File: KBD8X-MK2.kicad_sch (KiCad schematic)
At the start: 26 parts, among them J1 AVR-ISP-6, Q1 DSS60601MZ4-13, SW1 SW_Push, U1 ATmega32U4-MU, U2 PRTR5V0U2X, Y1 16MHz

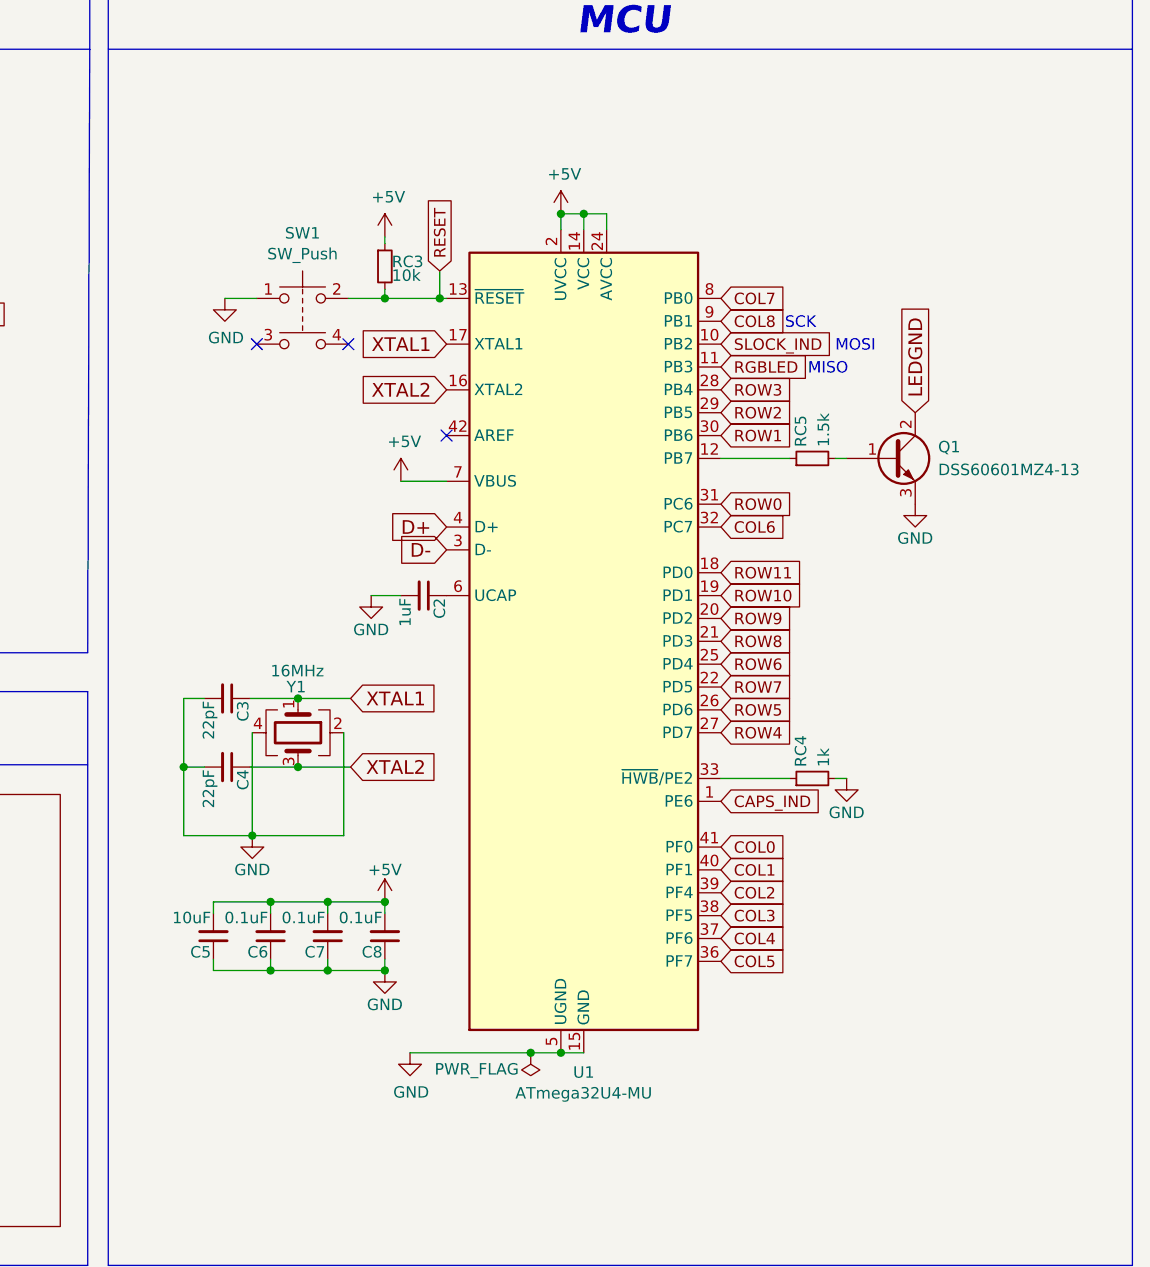
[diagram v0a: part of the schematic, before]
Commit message: Removed leds and unnecessary resistors
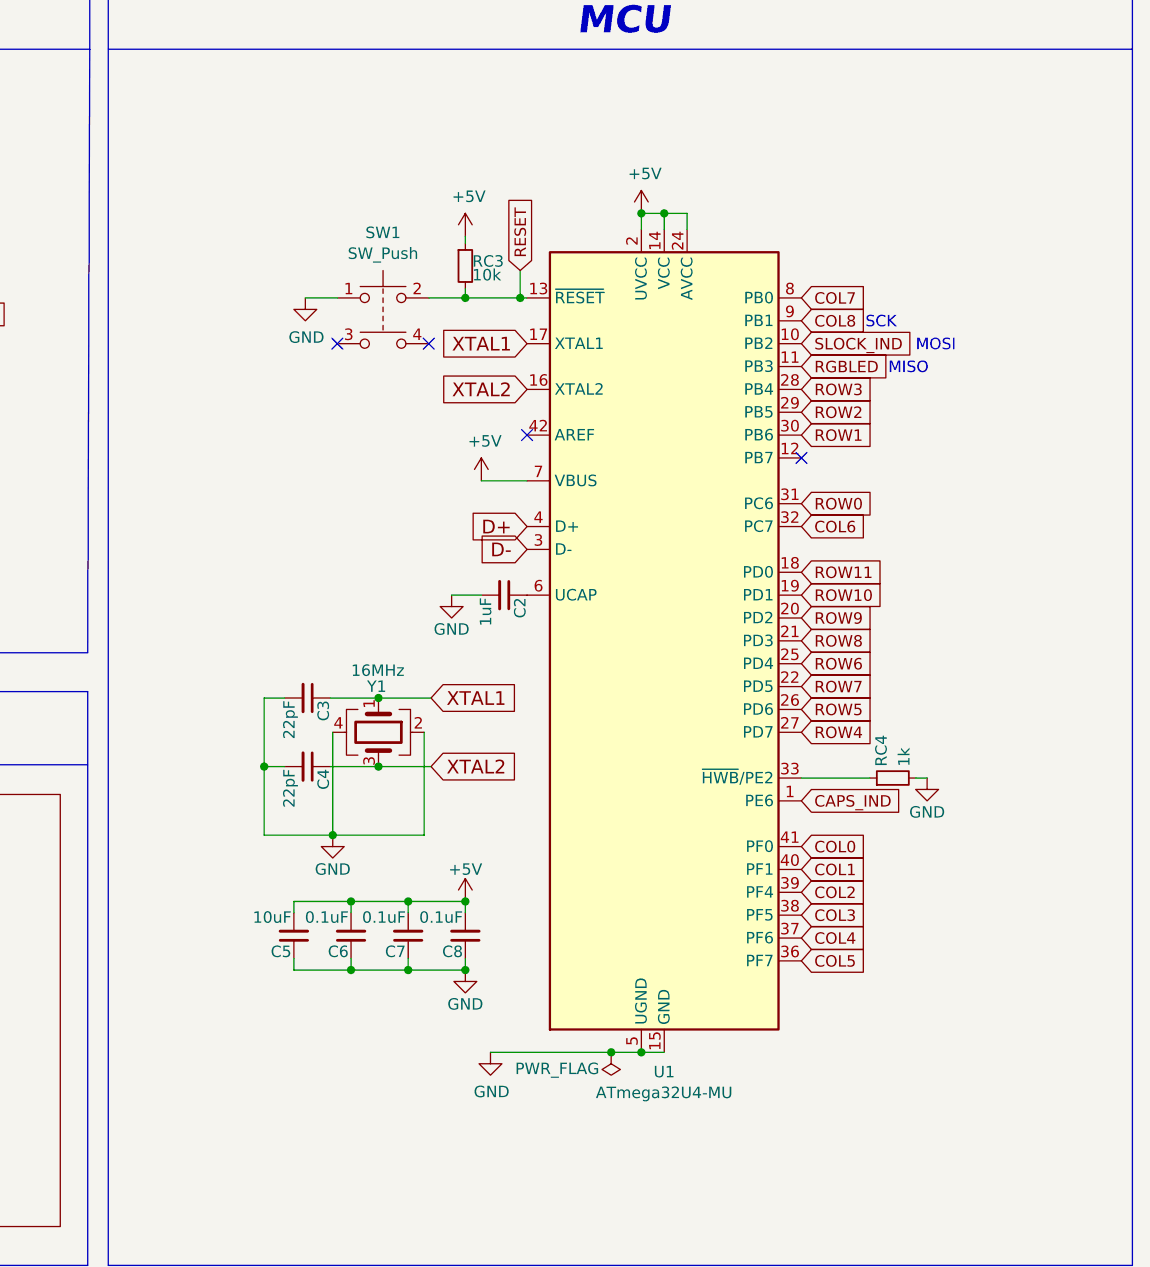
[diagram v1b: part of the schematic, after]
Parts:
- removed Q1: DSS60601MZ4-13, KBD8X_MK2_Components:SOT-223-3_TabPin2, symbol KBD8X_MK2_Components:Q_NPN_BCE
- removed RC5: 1.5k, KBD8X_MK2_Components:R_0603, symbol KBD8X_MK2_Components:R_Small
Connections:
- no-connect marks 5 -> 6
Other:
- moved on the sheet: C2, C3, C4, C5, C6, C7, C8, RC3, RC4, SW1, U1, Y1

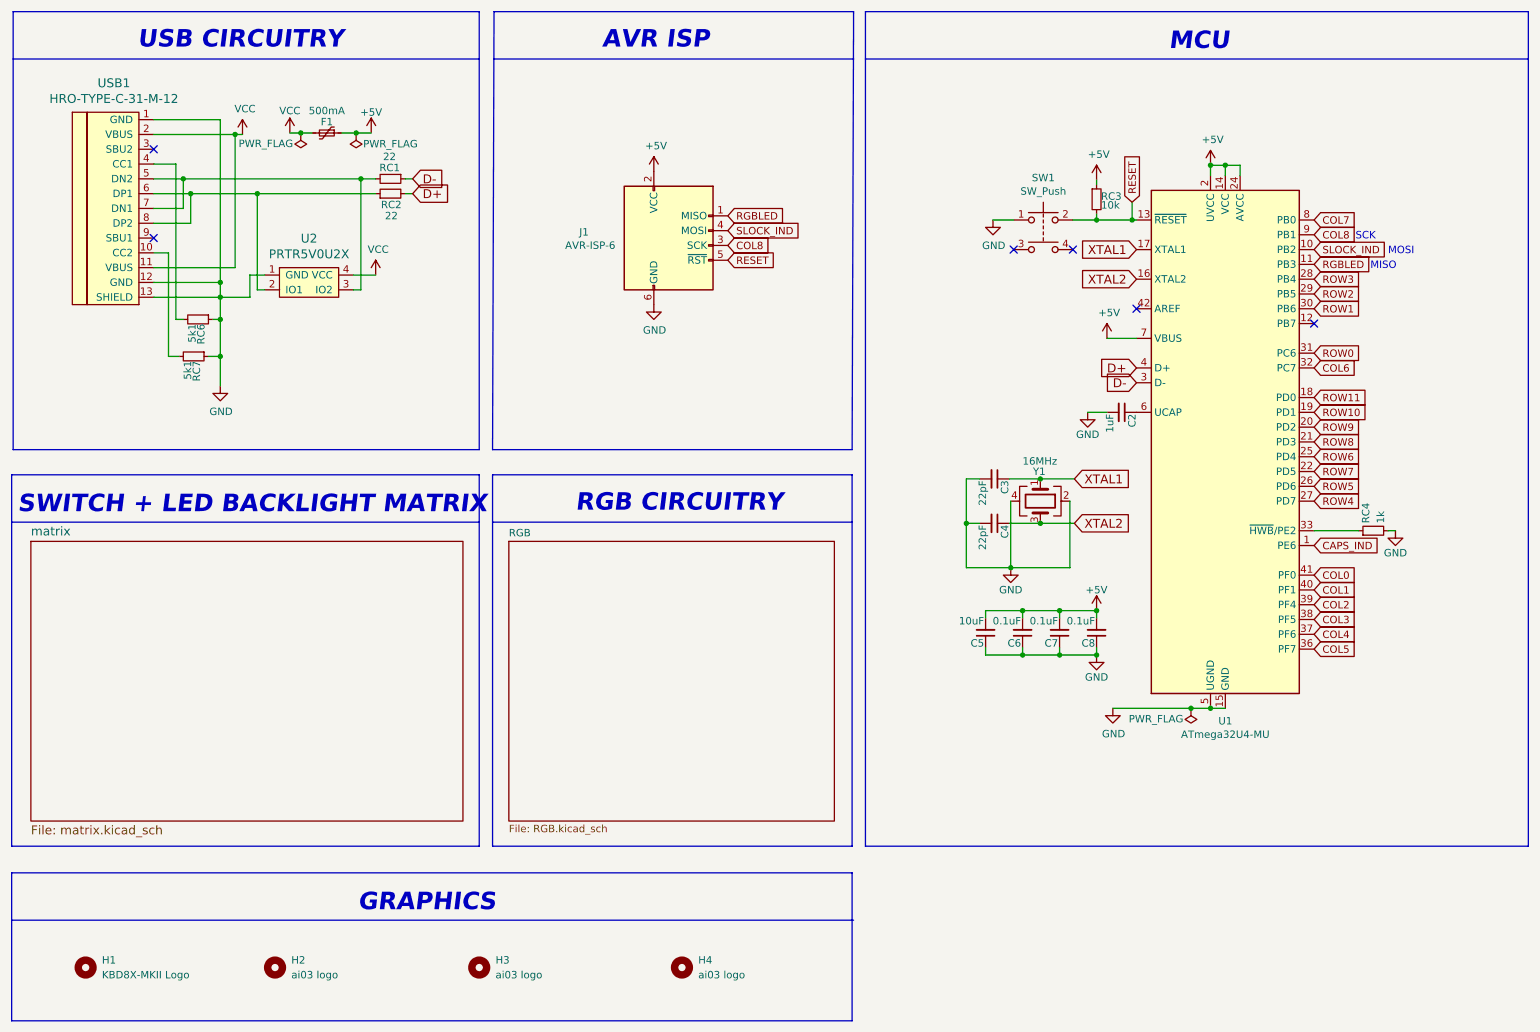
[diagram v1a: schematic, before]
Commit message: Removed everything related to RGB
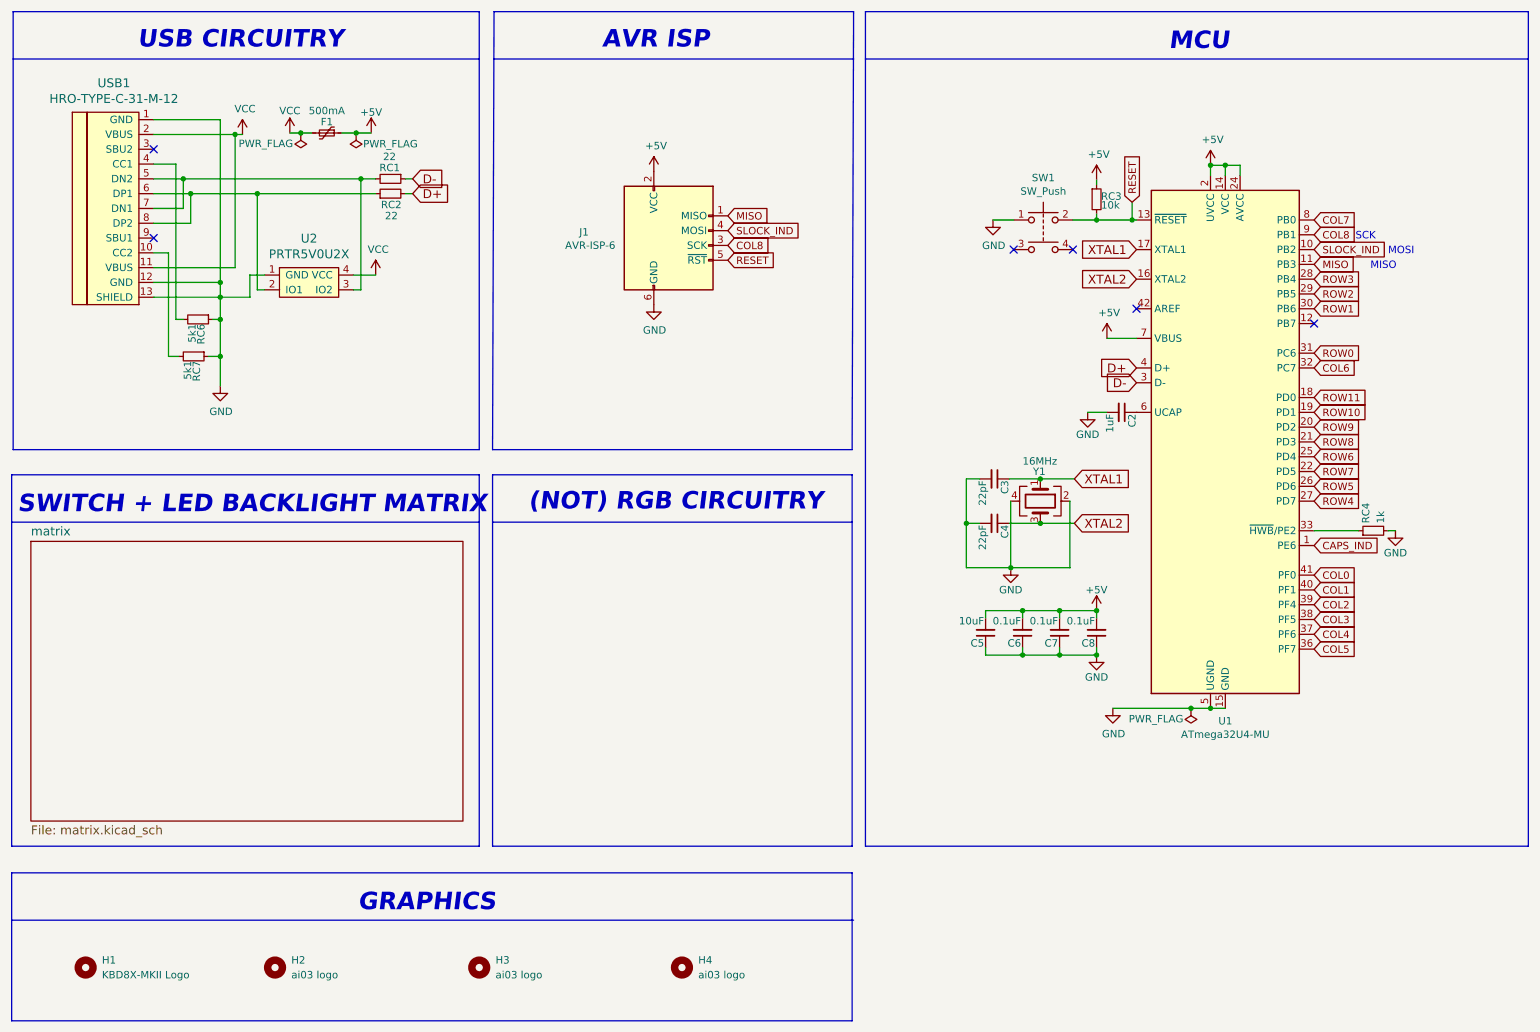
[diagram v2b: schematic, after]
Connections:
- net RGBLED renamed MISO
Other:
- removed sheet RGB
- note added: "(NOT) RGB CIRCUITRY"
- note removed: "RGB CIRCUITRY"
